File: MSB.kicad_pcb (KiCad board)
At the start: 2 copper layers, 39.1 x 40.6 mm, 25 parts, among them J1 22-05-3021, J2 22-05-3021, J3 90120-0763, J4 90120-0763, J5 22-05-3021, P1 22-27-2041, P2 22-27-2041, P3 61300811121, Q1 FDN5632N-F085, Q2 FDN5632N-F085, U1 MSP430FR2355TPTR, U2 LD1117S33TR

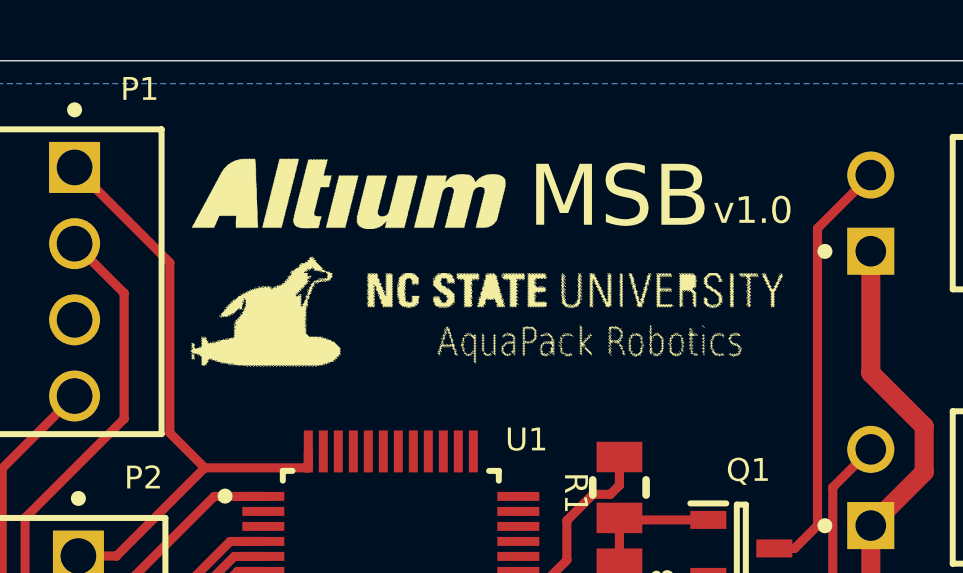
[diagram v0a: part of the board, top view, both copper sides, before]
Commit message: Fix footprint linking and logos
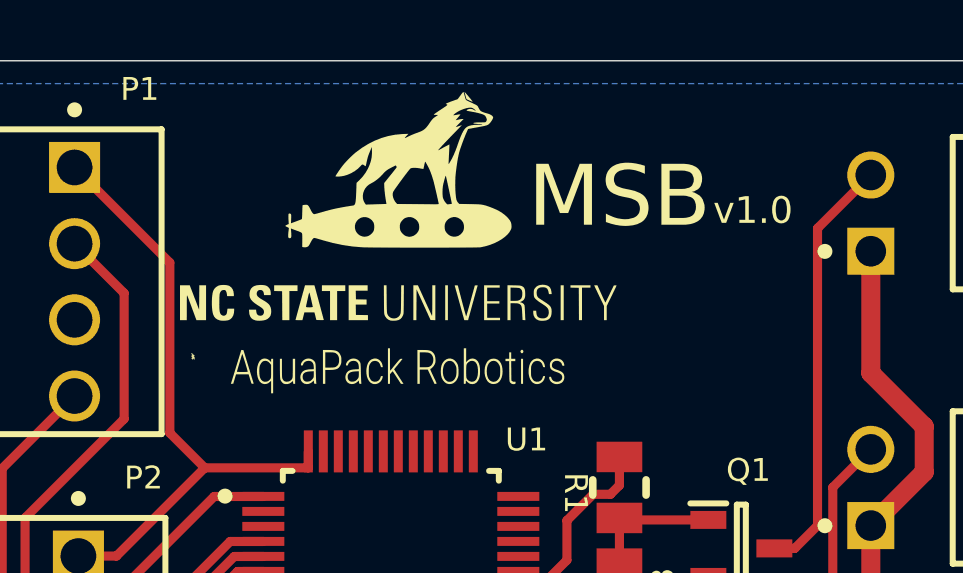
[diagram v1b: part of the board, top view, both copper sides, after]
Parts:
- added G***: LOGO, LOGO, F.Cu at (146.0, 90.8)

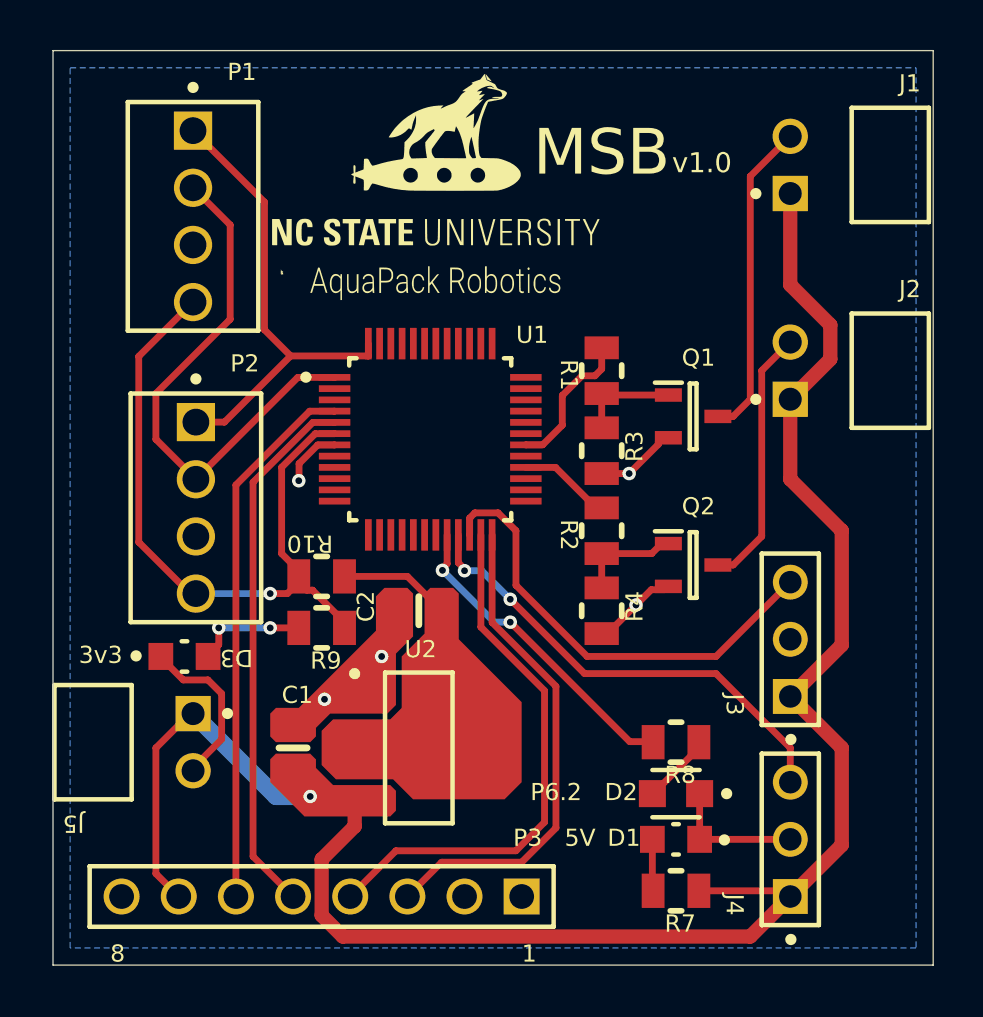
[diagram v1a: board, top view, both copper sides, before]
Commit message: Fix polygons, silkscreen, and other DRC issues
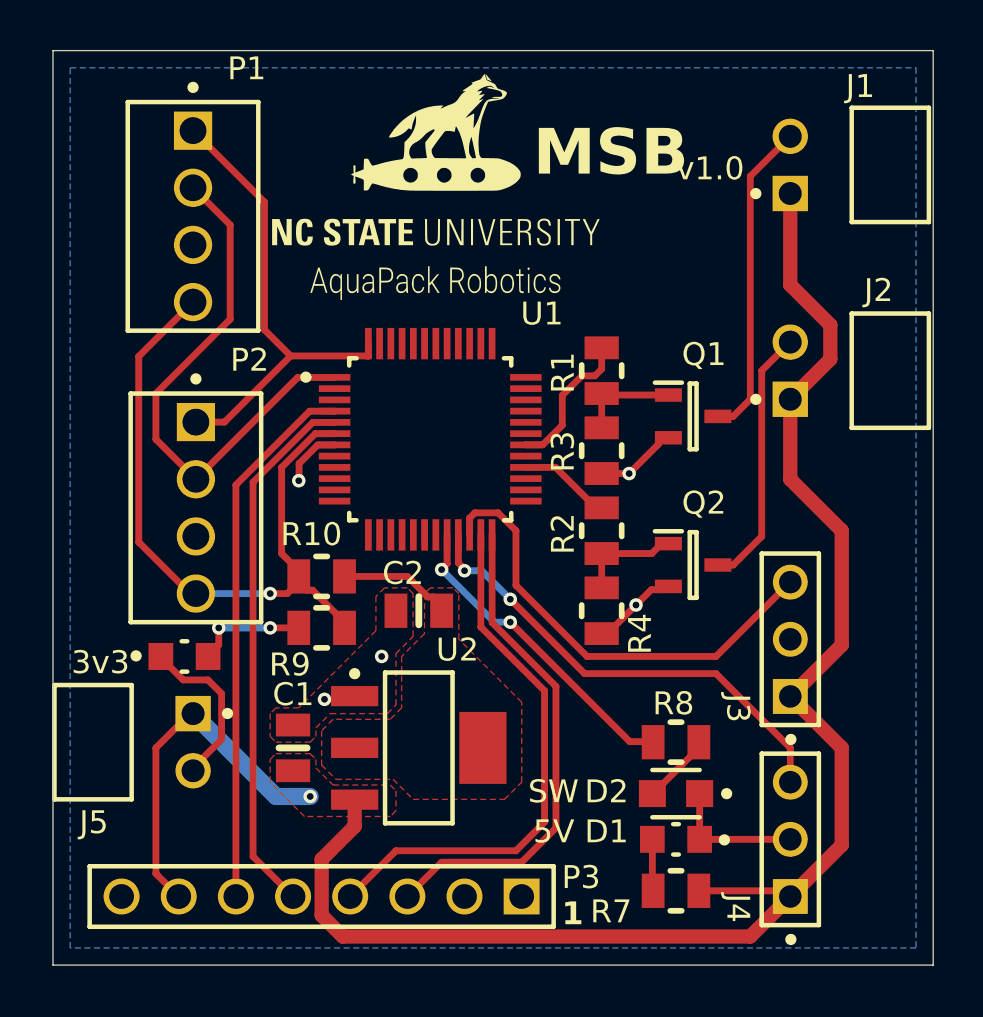
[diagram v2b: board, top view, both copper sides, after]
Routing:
- added copper zone on F.Cu, net +5
- added copper zone on F.Cu, net GND
- added copper zone on F.Cu, net Net-(C2-Pad1)
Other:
- rule pad_to_mask_clearance: 0 -> 0.05
- board text added: "SW"
- board text removed: "P6.2"

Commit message: v2
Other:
- board text added: "v2.0"
- board text removed: "v1.0"

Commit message: Update STM32
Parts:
- added U3: STM32L051C6Tx, Package_QFP:LQFP-48_7x7mm_P0.5mm, F.Cu at (145.8, 102.1)
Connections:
- J3 pad 3: /SERVO1_CTRL -> +5
- P3 pad 3: /RXD -> unconnected-(P3-Pad3)
- P3 pad 4: /TXD -> +5
- P3 pad 5: /RST -> unconnected-(P3-Pad5)
- P3 pad 6: /TST -> unconnected-(P3-Pad6)
- R8 pad 1: Net-(U1-P6.2/TB3.3) -> unconnected-(R8-Pad1)
